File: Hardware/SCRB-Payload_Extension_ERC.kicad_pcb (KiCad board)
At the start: 4 copper layers, 83 parts, among them J1 Conn_01x03, J2 Conn_LoadCell, J3 ST_Link_Conn, J4 Conn_LoadCell, J5 Conn_LoadCell, J7 Conn_Therm, Q1 NMOS, SW1 SW_Tiny, U1 STM32F412RET6, U2 TPD4E05U06DQAR, U3 THVD1500DR, U4 ADS1220IPW, U5 ADS1220IPW, U6 ADS1220IPW, U7 INA241xxIDDFR, U8 TPD4E05U06DQAR, Y1 16M, 9p

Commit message: Updated ERC board schematic
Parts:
- added C1: 0.1uF, SCRB_STD_Passives:C0402, F.Cu at (227.9, 122.3)
- added C10: 510pF, SCRB_STD_Passives:C0402, F.Cu at (230.4, 123.9)
- added C11: 510nF, SCRB_STD_Passives:C0402, F.Cu at (230.4, 125.5)
- added C12: 0.1uF, SCRB_STD_Passives:C0402, F.Cu at (230.4, 127.1)
- added C13: 510pF, SCRB_STD_Passives:C0402, F.Cu at (230.4, 128.7)
- added C14: 0.1uF, SCRB_STD_Passives:C0402, F.Cu at (230.4, 130.4)
- added C15: 5.1nF, SCRB_STD_Passives:C0402, F.Cu at (230.4, 132.0)
- added C16: 12p, SCRB_STD_Passives:C0402, F.Cu at (232.9, 122.3)
- added C17: 510pF, SCRB_STD_Passives:C0402, F.Cu at (232.9, 123.9)
- added C19: 4.7uF, SCRB_STD_Passives:C0603, F.Cu at (212.4, 129.3)
- added C2: 0.1uF, SCRB_STD_Passives:C0402, F.Cu at (227.9, 123.9)
- added C20: 0.1u, SCRB_STD_Passives:C0402, F.Cu at (232.9, 125.5)
- added C21: 12p, SCRB_STD_Passives:C0402, F.Cu at (232.9, 127.1)
- added C24: 510pF, SCRB_STD_Passives:C0402, F.Cu at (232.9, 128.7)
- added C25: 5.1nF, SCRB_STD_Passives:C0402, F.Cu at (232.9, 130.4)
- added C26: 510pF, SCRB_STD_Passives:C0402, F.Cu at (232.9, 132.0)
- added C27: 0.1uF, SCRB_STD_Passives:C0402, F.Cu at (235.4, 122.3)
- added C28: 16nF, SCRB_STD_Passives:C0402, F.Cu at (235.4, 123.9)
- added C29: 0.1uF, SCRB_STD_Passives:C0402, F.Cu at (235.4, 125.5)
- added C3: 4.7uF, SCRB_STD_Passives:C0603, F.Cu at (212.4, 127.4)
- added C30: 0.1uF, SCRB_STD_Passives:C0402, F.Cu at (235.4, 127.1)
- added C31: 10nF, SCRB_STD_Passives:C0402, F.Cu at (235.4, 128.7)
- added C4: 0.1uF, SCRB_STD_Passives:C0402, F.Cu at (227.9, 125.5)
- added C5: 0.1uF, SCRB_STD_Passives:C0402, F.Cu at (227.9, 127.1)
- added C6: 0.1uF, SCRB_STD_Passives:C0402, F.Cu at (227.9, 128.7)
- added C7: 0.1uF, SCRB_STD_Passives:C0402, F.Cu at (227.9, 130.4)
- added C8: 6.8nF, SCRB_STD_Passives:C0402, F.Cu at (227.9, 132.0)
- added C9: 5.1nF, SCRB_STD_Passives:C0402, F.Cu at (230.4, 122.3)
- added H1: MountingHole, MountingHole:MountingHole_3.2mm_M3_DIN965_Pad, F.Cu at (196.3, 97.0)
- added H2: MountingHole, MountingHole:MountingHole_3.2mm_M3_DIN965_Pad, F.Cu at (196.3, 104.2)
- added H3: MountingHole, MountingHole:MountingHole_3.2mm_M3_DIN965_Pad, F.Cu at (196.3, 111.3)
- added H4: MountingHole, MountingHole:MountingHole_3.2mm_M3_DIN965_Pad, F.Cu at (196.3, 118.5)
- added IC1: STM32C542CCT6, SCRB_Misc_ICs:LQFP-48_7x7mm_P0.5mm, F.Cu at (205.3, 131.8)
- added J1: Conn_01x03, Connector_JST:JST_XH_B3B-XH-A_1x03_P2.50mm_Vertical, F.Cu at (217.8, 132.1)
- added J11: Conn_5V, SCRB_STD_Passives:R0402, F.Cu at (224.8, 108.7)
- added J2: Conn_LoadCell, Connector_JST:JST_XH_B4B-XH-A_1x04_P2.50mm_Vertical, F.Cu at (203.4, 96.8)
- added J4: Conn_LoadCell, Connector_JST:JST_XH_B4B-XH-A_1x04_P2.50mm_Vertical, F.Cu at (203.4, 104.6)
- added J5: Conn_LoadCell, Connector_JST:JST_XH_B4B-XH-A_1x04_P2.50mm_Vertical, F.Cu at (203.4, 112.4)
- added J7: Conn_Therm, Connector_JST:JST_GH_BM02B-GHS-TBT_1x02-1MP_P1.25mm_Vertical, F.Cu at (232.8, 97.3)
- added J8: ST-Link-Conn-SM, Connector_JST:JST_PH_B4B-PH-SM4-TB_1x04-1MP_P2.00mm_Vertical, F.Cu at (207.1, 122.1)
- added J9: Conn_20HIGH, Connector_AMASS:AMASS_XT30U-M_1x02_P5.0mm_Vertical, F.Cu at (218.0, 125.1)
- added LD1: LED0603, SCRB_STD_Actives:LED0603, F.Cu at (212.4, 131.3)
- added LD2: LED0603, SCRB_STD_Actives:LED0603, F.Cu at (212.4, 133.2)
- added Q1: NMOS, SCRB_STD_Actives:SOT-23, F.Cu at (228.8, 134.7)
- added R1: 10k, SCRB_STD_Passives:R0402, F.Cu at (224.8, 110.4)
- added R10: 470, SCRB_STD_Passives:R0402, F.Cu at (227.3, 113.7)
- added R11: 10k, SCRB_STD_Passives:R0402, F.Cu at (227.3, 115.3)
- added R12: 47, SCRB_STD_Passives:R0402, F.Cu at (227.3, 116.9)
- added R13: 47, SCRB_STD_Passives:R0402, F.Cu at (229.9, 108.7)
- added R14: 47, SCRB_STD_Passives:R0402, F.Cu at (229.9, 110.4)
- added R15: 47, SCRB_STD_Passives:R0402, F.Cu at (229.9, 112.0)
- added R16: 47, SCRB_STD_Passives:R0402, F.Cu at (229.9, 113.7)
- added R17: 47, SCRB_STD_Passives:R0402, F.Cu at (229.9, 115.3)
- added R18: 47, SCRB_STD_Passives:R0402, F.Cu at (229.9, 116.9)
- added R19: 47, SCRB_STD_Passives:R0402, F.Cu at (232.4, 108.7)
- added R2: 120, SCRB_STD_Passives:R0805, F.Cu at (225.4, 119.0)
- added R20: 47, SCRB_STD_Passives:R0402, F.Cu at (232.4, 110.4)
- added R21: 47, SCRB_STD_Passives:R0402, F.Cu at (232.4, 112.0)
- added R22: 47, SCRB_STD_Passives:R0402, F.Cu at (232.4, 113.7)
- added R23: 47, SCRB_STD_Passives:R0402, F.Cu at (232.4, 115.3)
- added R24: 4.7k, SCRB_STD_Passives:R0402, F.Cu at (232.4, 116.9)
- added R25: 4.7k, SCRB_STD_Passives:R0402, F.Cu at (235.0, 108.7)
- added R26: 470, SCRB_STD_Passives:R0402, F.Cu at (235.0, 110.4)
- added R27: 10k, SCRB_STD_Passives:R0402, F.Cu at (235.0, 112.0)
- added R28: 100, SCRB_STD_Passives:R0402, F.Cu at (235.0, 113.7)
- added R29: 270, SCRB_STD_Passives:R0402, F.Cu at (235.0, 115.3)
- added R3: 470, SCRB_STD_Passives:R0402, F.Cu at (224.8, 112.0)
- added R30: 10m, SCRB_STD_Passives:R0603, F.Cu at (212.4, 135.2)
- added R31: 470, SCRB_STD_Passives:R0402, F.Cu at (235.0, 116.9)
- added R4: 470, SCRB_STD_Passives:R0402, F.Cu at (224.8, 113.7)
- added R5: 100, SCRB_STD_Passives:R0402, F.Cu at (224.8, 115.3)
- added R6: 100, SCRB_STD_Passives:R0402, F.Cu at (224.8, 116.9)
- added R7: 10k, SCRB_STD_Passives:R0402, F.Cu at (227.3, 108.7)
- added R8: 4.7k, SCRB_STD_Passives:R0402, F.Cu at (227.3, 110.4)
- added R9: 470, SCRB_STD_Passives:R0402, F.Cu at (227.3, 112.0)
- added SW1: SW_Tiny, SCRB_Electromechanical:SW_C913791, F.Cu at (194.8, 135.6)
- added TP1: Testpoint, TestPoint:TestPoint_Loop_D2.60mm_Drill1.6mm_Beaded, F.Cu at (195.3, 124.6)
- added U1: STM32F412RET6, Package_QFP:LQFP-64_10x10mm_P0.5mm, F.Cu at (221.6, 100.7)
- added U2: TPD4E05U06DQAR, SCRB_TexasInstruments:DQA0010A, F.Cu at (193.9, 128.9)
- added U3: THVD1500DR, SCRB_TexasInstruments:D0008A, F.Cu at (232.8, 104.1)
- added U4: ADS1220IPW, ADS1220:PW16, F.Cu at (218.8, 111.3)
- added U5: ADS1220IPW, ADS1220:PW16, F.Cu at (218.8, 118.1)
- added U7: INA241A4IDDFR, SCRB_TexasInstruments:DDF0008A, F.Cu at (233.1, 134.7)
- added U8: TPD4E05U06DQAR, SCRB_TexasInstruments:DQA0010A, F.Cu at (196.3, 128.9)
- added Y1: 16M, 9p, SCRB_STD_Passives:SMD3225, F.Cu at (195.1, 132.5)

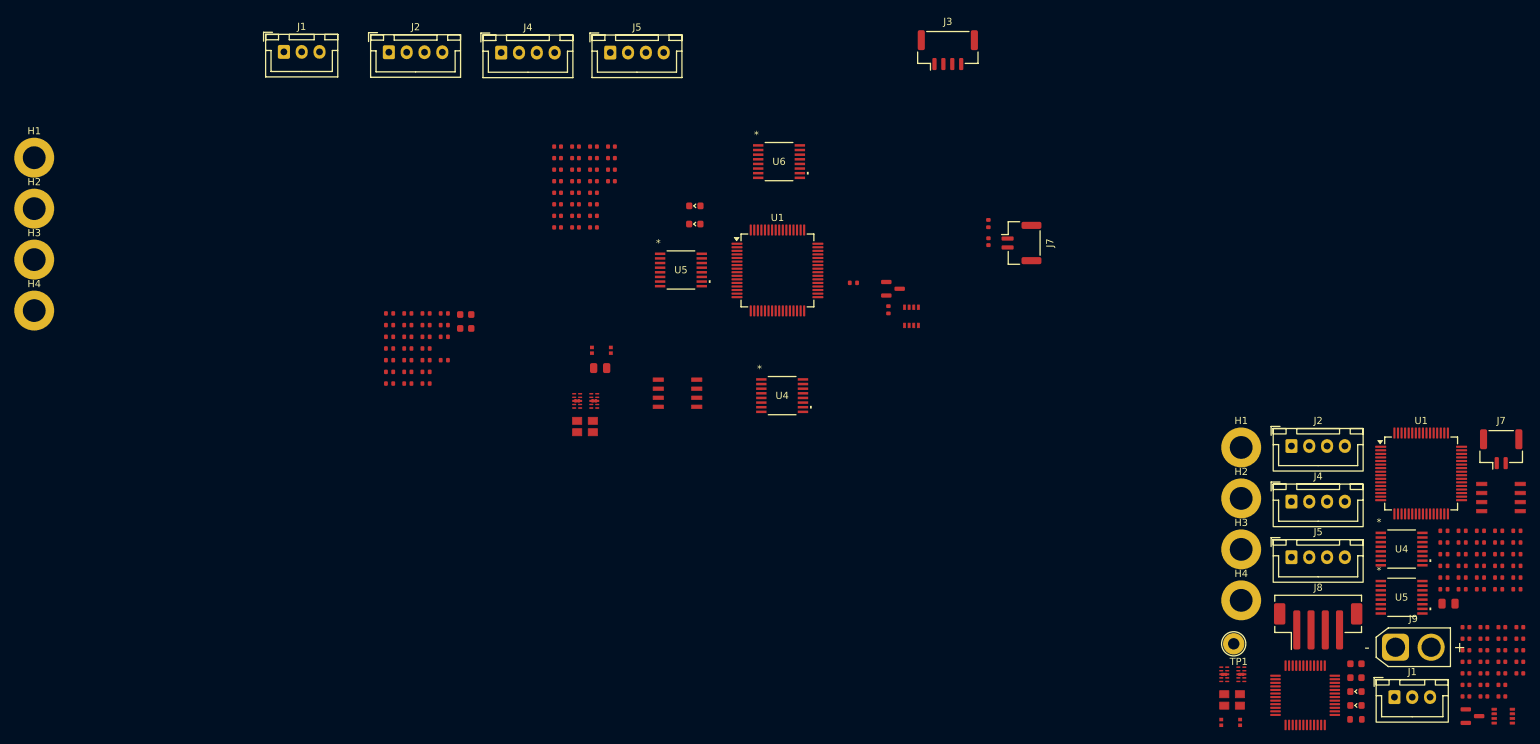
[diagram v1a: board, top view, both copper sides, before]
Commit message: added extra load cell on schematic
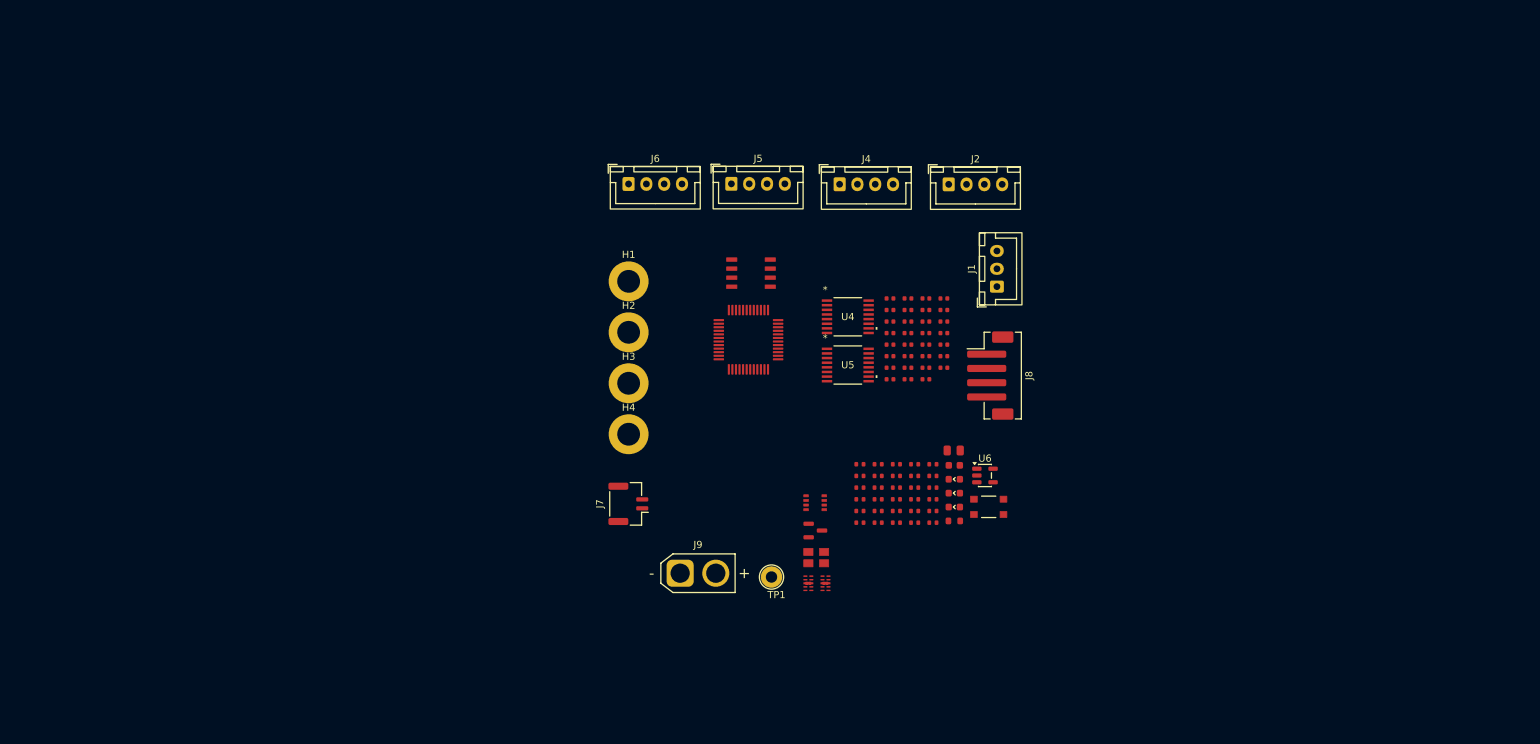
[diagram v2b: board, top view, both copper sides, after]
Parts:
- removed the C1 at (227.9, 122.3)
- removed the C1 at (100.4, 54.8)
- removed the C10 at (230.4, 123.9)
- removed the C10 at (102.9, 54.8)
- removed the C11 at (102.9, 56.5)
- removed the C11 at (230.4, 125.5)
- removed the C12 at (230.4, 127.1)
- removed the C12 at (102.9, 58.1)
- removed the C13 at (230.4, 128.7)
- removed the C13 at (102.9, 59.7)
- removed C14 (x2), C4 (x2), C5 (x2), C6 (x2): 0.1uF, SCRB_STD_Passives:C0402
- removed the C15 at (230.4, 132.0)
- removed the C15 at (102.9, 62.9)
- removed the C16 at (232.9, 122.3)
- removed the C16 at (102.9, 64.5)
- removed the C17 at (232.9, 123.9)
- removed the C17 at (102.9, 66.2)
- removed C19 (x2), C3 (x2): 4.7uF, SCRB_STD_Passives:C0603
- removed the C2 at (227.9, 123.9)
- removed the C2 at (100.4, 56.5)
- removed the C20 at (232.9, 125.5)
- removed the C20 at (105.5, 56.5)
- removed the C21 at (232.9, 127.1)
- removed the C21 at (105.5, 58.1)
- removed the C24 at (105.5, 62.9)
- removed the C24 at (232.9, 128.7)
- removed the C25 at (232.9, 130.4)
- removed the C25 at (105.5, 64.5)
- removed the C26 at (232.9, 132.0)
- removed the C26 at (105.5, 66.2)
- removed the C27 at (108.0, 54.8)
- removed the C27 at (235.4, 122.3)
- removed C28: 16nF, SCRB_STD_Passives:C0402
- removed C28: 5.1nF, SCRB_STD_Passives:C0402
- removed the C29 at (108.0, 58.1)
- removed the C29 at (235.4, 125.5)
- removed the C30 at (108.0, 59.7)
- removed the C30 at (235.4, 127.1)
- removed the C31 at (160.9, 68.2)
- removed the C31 at (235.4, 128.7)
- removed the C7 at (227.9, 130.4)
- removed the C7 at (100.4, 62.9)
- removed the C8 at (100.4, 64.5)
- removed the C8 at (227.9, 132.0)
- removed the C9 at (230.4, 122.3)
- removed the C9 at (100.4, 66.2)
- removed the H1 at (27.0, 56.4)
- removed the H1 at (196.3, 97.0)
- removed the H2 at (27.0, 63.5)
- removed the H2 at (196.3, 104.2)
- removed the H3 at (27.0, 70.7)
- removed the H3 at (196.3, 111.3)
- removed the H4 at (196.3, 118.5)
- removed the H4 at (27.0, 77.8)
- removed the J1 at (217.8, 132.1)
- removed the J1 at (62.0, 41.5)
- removed the J2 at (203.4, 96.8)
- removed the J2 at (76.7, 41.6)
- removed J3: ST_Link_Conn, Connector_JST:JST_GH_BM04B-GHS-TBT_1x04-1MP_P1.25mm_Vertical
- removed the J4 at (203.4, 104.6)
- removed the J4 at (92.5, 41.6)
- removed the J5 at (107.8, 41.6)
- removed the J5 at (203.4, 112.4)
- removed the J7 at (232.8, 97.3)
- removed the J7 at (165.5, 68.4)
- removed the LD1 at (119.7, 63.1)
- removed the LD1 at (212.4, 131.3)
- removed the LD2 at (212.4, 133.2)
- removed the LD2 at (119.7, 65.7)
- removed the Q1 at (228.8, 134.7)
- removed the Q1 at (147.5, 74.8)
- removed the R1 at (76.8, 78.2)
- removed the R1 at (224.8, 110.4)
- removed the R10 at (79.4, 79.9)
- removed the R10 at (227.3, 113.7)
- removed the R11 at (227.3, 115.3)
- removed the R11 at (79.4, 81.5)
- removed the R12 at (79.4, 83.2)
- removed the R12 at (227.3, 116.9)
- removed R13 (x2), R14 (x2), R15 (x2), R16 (x2), R17 (x2), R18 (x2), R19 (x2), R20 (x2), R21 (x2), R22 (x2), R23 (x2): 47, SCRB_STD_Passives:R0402
- removed the R2 at (225.4, 119.0)
- removed the R2 at (106.4, 85.9)
- removed R24 (x2), R25 (x2): 4.7k, SCRB_STD_Passives:R0402
- removed the R26 at (146.8, 77.7)
- removed the R26 at (235.0, 110.4)
- removed the R27 at (235.0, 112.0)
- removed the R27 at (84.5, 84.8)
- removed the R28 at (141.9, 74.0)
- removed the R28 at (235.0, 113.7)
- removed the R29 at (235.0, 115.3)
- removed the R29 at (160.9, 65.6)
- removed the R3 at (224.8, 112.0)
- removed the R3 at (76.8, 79.9)
- removed the R4 at (224.8, 113.7)
- removed the R4 at (76.8, 81.5)
- removed the R5 at (224.8, 115.3)
- removed the R5 at (76.8, 83.2)
- removed the R6 at (224.8, 116.9)
- removed the R6 at (76.8, 84.8)
- removed the R7 at (76.8, 86.4)
- removed the R7 at (227.3, 108.7)
- removed the R8 at (76.8, 88.1)
- removed the R8 at (227.3, 110.4)
- removed the R9 at (227.3, 112.0)
- removed the R9 at (79.4, 78.2)
- removed the SW1 at (106.6, 83.4)
- removed the SW1 at (194.8, 135.6)
- removed U1 (x2): STM32F412RET6, Package_QFP:LQFP-64_10x10mm_P0.5mm
- removed the U2 at (193.9, 128.9)
- removed the U2 at (103.2, 90.5)
- removed the U3 at (117.2, 89.4)
- removed the U3 at (232.8, 104.1)
- removed the U4 at (218.8, 111.3)
- removed the U4 at (131.9, 89.8)
- removed the U5 at (218.8, 118.1)
- removed the U5 at (117.7, 72.1)
- removed the U7 at (150.1, 78.7)
- removed the U7 at (233.1, 134.7)
- removed the U8 at (105.6, 90.5)
- removed the U8 at (196.3, 128.9)
- removed the Y1 at (195.1, 132.5)
- removed the Y1 at (104.3, 94.1)
- added C1: 0.1uF, SCRB_STD_Passives:C0402, F.Cu at (147.1, 76.1)
- added C10: 510pF, SCRB_STD_Passives:C0402, F.Cu at (147.1, 84.2)
- added C11: 510nF, SCRB_STD_Passives:C0402, F.Cu at (147.1, 85.9)
- added C12: 6.8nF, SCRB_STD_Passives:C0402, F.Cu at (147.1, 87.5)
- added C13: 510pF, SCRB_STD_Passives:C0402, F.Cu at (149.6, 76.1)
- added C15: 5.1nF, SCRB_STD_Passives:C0402, F.Cu at (149.6, 77.8)
- added C16: 12p, SCRB_STD_Passives:C0402, F.Cu at (149.6, 79.4)
- added C17: 510pF, SCRB_STD_Passives:C0402, F.Cu at (149.6, 81.0)
- added C2: 0.1uF, SCRB_STD_Passives:C0402, F.Cu at (147.1, 77.8)
- added C20: 0.1u, SCRB_STD_Passives:C0402, F.Cu at (149.6, 84.2)
- added C21: 12p, SCRB_STD_Passives:C0402, F.Cu at (149.6, 85.9)
- added C24: 510pF, SCRB_STD_Passives:C0402, F.Cu at (152.1, 77.8)
- added C25: 5.1nF, SCRB_STD_Passives:C0402, F.Cu at (152.1, 79.4)
- added C26: 510pF, SCRB_STD_Passives:C0402, F.Cu at (152.1, 81.0)
- added C27: 0.1uF, SCRB_STD_Passives:C0402, F.Cu at (152.1, 82.6)
- added C29: 0.1uF, SCRB_STD_Passives:C0402, F.Cu at (152.1, 84.2)
- added C30: 0.1uF, SCRB_STD_Passives:C0402, F.Cu at (152.1, 85.9)
- added C31: 510pF, SCRB_STD_Passives:C0402, F.Cu at (152.1, 87.5)
- added C32: 0.1uF, SCRB_STD_Passives:C0402, F.Cu at (154.6, 76.1)
- added C33: 0.1unF, SCRB_STD_Passives:C0402, F.Cu at (154.6, 77.8)
- added C34: 4.7uF, SCRB_STD_Passives:C0402, F.Cu at (154.6, 79.4)
- added C35: 2.2uF, SCRB_STD_Passives:C0603, F.Cu at (156.1, 99.6)
- added C36: 0.1uF, SCRB_STD_Passives:C0402, F.Cu at (154.6, 81.0)
- added C37: 10nF, SCRB_STD_Passives:C0402, F.Cu at (154.6, 82.6)
- added C38: 5.1nF, SCRB_STD_Passives:C0402, F.Cu at (154.6, 84.2)
- added C39: 510pF, SCRB_STD_Passives:C0402, F.Cu at (154.6, 85.9)
- added C7: 0.1uF, SCRB_STD_Passives:C0402, F.Cu at (147.1, 79.4)
- added C8: 6.8nF, SCRB_STD_Passives:C0402, F.Cu at (147.1, 81.0)
- added C9: 5.1nF, SCRB_STD_Passives:C0402, F.Cu at (147.1, 82.6)
- added H1: MountingHole, MountingHole:MountingHole_3.2mm_M3_DIN965_Pad, F.Cu at (110.4, 73.7)
- added H2: MountingHole, MountingHole:MountingHole_3.2mm_M3_DIN965_Pad, F.Cu at (110.4, 80.9)
- added H3: MountingHole, MountingHole:MountingHole_3.2mm_M3_DIN965_Pad, F.Cu at (110.4, 88.0)
- added H4: MountingHole, MountingHole:MountingHole_3.2mm_M3_DIN965_Pad, F.Cu at (110.4, 95.2)
- added J1: Conn_01x03, Connector_JST:JST_XH_B3B-XH-A_1x03_P2.50mm_Vertical, F.Cu at (162.1, 74.5)
- added J2: Conn_LoadCell, Connector_JST:JST_XH_B4B-XH-A_1x04_P2.50mm_Vertical, F.Cu at (155.3, 60.1)
- added J4: Conn_LoadCell, Connector_JST:JST_XH_B4B-XH-A_1x04_P2.50mm_Vertical, F.Cu at (140.0, 60.1)
- added J5: Conn_LoadCell, Connector_JST:JST_XH_B4B-XH-A_1x04_P2.50mm_Vertical, F.Cu at (124.8, 60.1)
- added J6: Conn_LoadCell, Connector_JST:JST_XH_B4B-XH-A_1x04_P2.50mm_Vertical, F.Cu at (110.4, 60.1)
- added J7: Conn_Therm, Connector_JST:JST_GH_BM02B-GHS-TBT_1x02-1MP_P1.25mm_Vertical, F.Cu at (110.3, 105.0)
- added LD1: LED0603, SCRB_STD_Actives:LED0603, F.Cu at (156.1, 101.5)
- added LD2: LED0603, SCRB_STD_Actives:LED0603, F.Cu at (156.1, 103.5)
- added LD3: LED0603, SCRB_STD_Actives:LED0603, F.Cu at (156.1, 105.4)
- added Q1: NMOS, SCRB_STD_Actives:SOT-23, F.Cu at (136.6, 108.7)
- added R1: 10k, SCRB_STD_Passives:R0402, F.Cu at (142.8, 101.0)
- added R10: 470, SCRB_STD_Passives:R0402, F.Cu at (145.4, 104.3)
- added R11: 470, SCRB_STD_Passives:R0402, F.Cu at (145.4, 106.0)
- added R12: 470, SCRB_STD_Passives:R0402, F.Cu at (145.4, 107.6)
- added R2: 120, SCRB_STD_Passives:R0805, F.Cu at (156.0, 97.5)
- added R26: 470, SCRB_STD_Passives:R0402, F.Cu at (147.9, 99.4)
- added R27: 10k, SCRB_STD_Passives:R0402, F.Cu at (147.9, 101.0)
- added R28: 100, SCRB_STD_Passives:R0402, F.Cu at (147.9, 102.7)
- added R29: 270, SCRB_STD_Passives:R0402, F.Cu at (147.9, 104.3)
- added R3: 470, SCRB_STD_Passives:R0402, F.Cu at (142.8, 102.7)
- added R32: 10k, SCRB_STD_Passives:R0402, F.Cu at (147.9, 107.6)
- added R33: 47, SCRB_STD_Passives:R0402, F.Cu at (150.5, 99.4)
- added R34: 47, SCRB_STD_Passives:R0402, F.Cu at (150.5, 101.0)
- added R35: 47, SCRB_STD_Passives:R0402, F.Cu at (150.5, 102.7)
- added R36: 47, SCRB_STD_Passives:R0402, F.Cu at (150.5, 104.3)
- added R37: 47, SCRB_STD_Passives:R0402, F.Cu at (150.5, 106.0)
- added R38: 47, SCRB_STD_Passives:R0402, F.Cu at (150.5, 107.6)
- added R39: 47, SCRB_STD_Passives:R0402, F.Cu at (153.1, 99.4)
- added R4: 470, SCRB_STD_Passives:R0402, F.Cu at (142.8, 104.3)
- added R40: 47, SCRB_STD_Passives:R0402, F.Cu at (153.1, 101.0)
- added R41: 4.7K, SCRB_STD_Passives:R0402, F.Cu at (153.1, 102.7)
- added R42: 4.7K, SCRB_STD_Passives:R0402, F.Cu at (153.1, 104.3)
- added R43: 470, SCRB_STD_Passives:R0402, F.Cu at (153.1, 106.0)
- added R44: 470, SCRB_STD_Passives:R0402, F.Cu at (153.1, 107.6)
- added R5: 100, SCRB_STD_Passives:R0402, F.Cu at (142.8, 106.0)
- added R6: 100, SCRB_STD_Passives:R0402, F.Cu at (142.8, 107.6)
- added R7: 10k, SCRB_STD_Passives:R0402, F.Cu at (145.4, 99.4)
- added R8: 4.7k, SCRB_STD_Passives:R0402, F.Cu at (145.4, 101.0)
- added R9: 470, SCRB_STD_Passives:R0402, F.Cu at (145.4, 102.7)
- added SW1: SW_Oval, SCRB_Electromechanical:SW_C2888430, F.Cu at (160.9, 105.4)
- added U2: TPD4E05U06DQAR, SCRB_TexasInstruments:DQA0010A, F.Cu at (135.6, 116.1)
- added U3: THVD1500DR, SCRB_TexasInstruments:D0008A, F.Cu at (127.5, 72.6)
- added U4: ADS1220IPW, ADS1220:PW16, F.Cu at (141.1, 78.7)
- added U5: ADS1220IPW, ADS1220:PW16, F.Cu at (141.1, 85.5)
- added U7: INA241A4IDDFR, SCRB_TexasInstruments:DDF0008A, F.Cu at (136.6, 104.8)
- added U8: TPD4E05U06DQAR, SCRB_TexasInstruments:DQA0010A, F.Cu at (138.0, 116.1)
- added Y1: 16M, 9p, SCRB_STD_Passives:SMD3225, F.Cu at (136.7, 112.5)
- C18: value 0.1uF -> 1uF
- C22: value 5.1nF -> 0.1uF
- U6: value ADS1220IPW -> TLV75533PDBV; footprint ADS1220:PW16 -> Package_TO_SOT_SMD:SOT-23-5
- moved J9 100.9 mm to (117.6, 114.7)
- moved IC1 92.7 mm to (127.2, 81.9)
- moved R31 87.7 mm to (147.9, 106.0)
- moved J11 82.5 mm to (142.8, 99.4)
- moved TP1 65.5 mm to (130.4, 115.2)
- moved R30 62.9 mm to (156.1, 107.4)
- moved J8 57.9 mm to (161.1, 87.0), turned to -90 degrees
- moved U6 52.7 mm to (160.4, 101.0)
- moved C18 52.1 mm to (149.6, 82.6)
- moved C22 52.1 mm to (149.6, 87.5)
- moved C23 48.9 mm to (152.1, 76.1)
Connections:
- C22 pad 1: /5V -> /3V3
- C22 pad 2: /E2- -> GND
- C23 pad 1: /3V3 -> GND
- C23 pad 2: GND -> /3V3
- IC1 pad 1: unconnected-(IC1-PE2-Pad1) -> /LED_RUN
- IC1 pad 11: unconnected-(IC1-PA1-Pad11) -> /ADC_Therm
- IC1 pad 12: unconnected-(IC1-PA2-Pad12) -> /CURR_VOUT
- IC1 pad 13: unconnected-(IC1-PA3-Pad13) -> Net-(IC1-PA3)
- IC1 pad 14: unconnected-(IC1-PA4-Pad14) -> Net-(IC1-PA4)
- IC1 pad 15: unconnected-(IC1-PA5-Pad15) -> Net-(IC1-PA5)
- IC1 pad 16: unconnected-(IC1-PA6-Pad16) -> Net-(IC1-PA6)
- IC1 pad 17: unconnected-(IC1-PA7-Pad17) -> Net-(IC1-PA7)
- IC1 pad 19: unconnected-(IC1-PB1-Pad19) -> Net-(IC1-PB1)
- IC1 pad 2: unconnected-(IC1-PC13-Pad2) -> /LED_PANIK
- IC1 pad 20: unconnected-(IC1-PB2-Pad20) -> Net-(IC1-PB2)
- IC1 pad 21: unconnected-(IC1-PB10-Pad21) -> Net-(IC1-PB10)
- IC1 pad 22: unconnected-(IC1-VCAP-Pad22) -> Net-(IC1-VCAP)
- IC1 pad 23: unconnected-(IC1-VSS_1-Pad23) -> GND
- IC1 pad 24: unconnected-(IC1-VDD_1-Pad24) -> /3V3
- IC1 pad 25: unconnected-(IC1-PB12-Pad25) -> /UART_RX
- IC1 pad 26: unconnected-(IC1-PB13-Pad26) -> /UART_TX
- IC1 pad 29: unconnected-(IC1-PA8-Pad29) -> /GATE_SW
- IC1 pad 34: unconnected-(IC1-PA13-Pad34) -> /SYS_SWDIO
- IC1 pad 35: unconnected-(IC1-VSS_2-Pad35) -> GND
- IC1 pad 36: unconnected-(IC1-VDD_2-Pad36) -> /3V3
- IC1 pad 37: unconnected-(IC1-PA14-Pad37) -> /SYS_SWDCLK
- IC1 pad 47: unconnected-(IC1-VSS_3-Pad47) -> GND
- IC1 pad 48: unconnected-(IC1-VDD_3-Pad48) -> /3V3
- IC1 pad 5: unconnected-(IC1-PH0-OSC_IN-Pad5) -> /RCC_OSC_IN
- IC1 pad 6: unconnected-(IC1-PH1-OSC_OUT-Pad6) -> /RCC_OSC_OUT
- IC1 pad 7: unconnected-(IC1-NRST-Pad7) -> /NRST
- IC1 pad 8: unconnected-(IC1-VREF--Pad8) -> GND
- IC1 pad 9: unconnected-(IC1-VREF+-Pad9) -> Net-(IC1-VREF+)
- U6 pad 1: /SPI3_SCK -> /5V
- U6 pad 2: /SPI3_~{CS} -> GND
- U6 pad 3: GND -> /5V
- U6 pad 4: GND -> unconnected-(U6-NC-Pad4)
- U6 pad 5: GND -> /3V3

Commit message: working on buck converter wiring
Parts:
- added IC2: AOZ2260AQI-15, AOZ2260AQI-15:AOZ2260AQI15, F.Cu at (155.2, 70.1)
- R29: value 270 -> 680
- moved J2 37.5 mm to (119.0, 69.7)
- moved U3 36.1 mm to (119.5, 107.8)
- moved SW1 34.3 mm to (126.6, 107.0)
- moved J6 34.2 mm to (119.0, 93.1)
- moved J1 31.1 mm to (149.8, 103.1), turned to 0 degrees
- moved J7 30.8 mm to (141.1, 106.2), turned to 0 degrees
- moved U6 27.8 mm to (132.6, 102.4)
- moved IC1 27.4 mm to (151.7, 94.3)
- moved J4 27.3 mm to (119.0, 77.5)
- moved R2 26.9 mm to (131.9, 109.5)
- moved J5 25.9 mm to (119.0, 85.3)
- moved H1 23.5 mm to (133.6, 69.9)
- moved H2 23.5 mm to (133.6, 77.1)
- moved H3 23.5 mm to (133.6, 84.2)
- moved H4 23.5 mm to (133.6, 91.4)
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
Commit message: PCB layout in progress
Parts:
- removed C34: 4.7uF, SCRB_STD_Passives:C0402
- removed IC2: AOZ2260AQI-15, AOZ2260AQI-15:AOZ2260AQI15
- added C14: 0.1u, SCRB_STD_Passives:C0402, F.Cu at (205.5, 82.8)
- added C3: 10u, SCRB_STD_Passives:C0402, F.Cu at (192.1, 78.4)
- added C4: 68u, SCRB_STD_Passives:C0603, F.Cu at (189.2, 78.5)
- added C5: 20p, SCRB_STD_Passives:C0402, F.Cu at (192.1, 80.0)
- added C6: 4.7u, SCRB_STD_Passives:C0603, F.Cu at (125.0, 80.3)
- added D1: D_Zener, Diode_THT:D_DO-41_SOD81_P10.16mm_Horizontal, F.Cu at (186.7, 75.4)
- added D2: SMBJ6.0CA, SCRB_STD_Actives:SMB, F.Cu at (144.9, 104.9)
- added L1: 3.7u, SCRB_STD_Passives:L0805, F.Cu at (195.4, 78.7)
- added R13: 121k, SCRB_STD_Passives:R0402, F.Cu at (186.1, 78.4)
- added R14: 54.9k, SCRB_STD_Passives:R0402, F.Cu at (186.1, 80.0)
- added R15: 18k, SCRB_STD_Passives:R0402, F.Cu at (201.4, 79.9)
- added R16: 30k, SCRB_STD_Passives:R0603, F.Cu at (189.2, 80.5)
- added R17: 45k, SCRB_STD_Passives:R0603, F.Cu at (204.4, 80.7)
- added R18: 100k, SCRB_STD_Passives:R0402, F.Cu at (201.4, 81.6)
- added R19: R0402, SCRB_STD_Passives:R0402, F.Cu at (201.4, 83.2)
- added SB1: SB0402, SCRB_STD_Passives:JP0402_NO, F.Cu at (147.8, 98.7)
- added U1: TPS543x21, TPS54x38:VQFN-HR9_RQF_TEX, F.Cu at (204.0, 75.7)
- C33: value 0.1unF -> 0.1uF
- H1, H2, H3, H4: footprint MountingHole:MountingHole_3.2mm_M3_DIN965_Pad -> MountingHole:MountingHole_3.2mm_M3
- J1: value Conn_01x03 -> Conn_UART
- J11: footprint SCRB_STD_Passives:R0402 -> Connector_JST:JST_XH_B2B-XH-AM_1x02_P2.50mm_Vertical
- J2, J4, J5, J6: footprint Connector_JST:JST_XH_B4B-XH-A_1x04_P2.50mm_Vertical -> Connector_JST:JST_PH_B4B-PH-SM4-TB_1x04-1MP_P2.00mm_Vertical
- J9: value Conn_20HIGH -> Conn_6HIGH
- LD3: value LED0603 -> 3V3_LED
- moved J6 54.8 mm to (172.5, 104.8), turned to -90 degrees
- moved J5 53.8 mm to (172.5, 91.0), turned to -90 degrees
- moved J4 53.5 mm to (172.5, 77.2), turned to -90 degrees
- moved R41 53.4 mm to (117.5, 114.0), turned to 180 degrees
- moved H3 51.3 mm to (174.5, 115.2)
- moved R1 47.5 mm to (114.1, 111.1), turned to 180 degrees
- moved U8 45.0 mm to (125.5, 74.7), turned to -90 degrees
- moved LD2 42.3 mm to (118.0, 82.7), turned to 180 degrees
- moved LD1 42.2 mm to (118.0, 81.1), turned to 180 degrees
- moved H2 42.2 mm to (174.5, 66.9)
- moved J9 39.1 mm to (156.3, 113.4)
- moved J7 38.4 mm to (140.5, 67.8)
- moved Q1 38.1 mm to (158.7, 72.8)
- moved H4 37.9 mm to (104.1, 115.2)
- moved R8 36.5 mm to (114.8, 82.7)
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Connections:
- net /20_Hi renamed /6_Hi
- C22 pad 1: /3V3 -> /ldo_3V3
- J11 pad 1: /5V -> /tvs_5V
- J9 pad 2: 20_Lo -> GND
- R11 pad 1: unconnected-(R11-Pad1) -> /Sig4+
- R12 pad 1: unconnected-(R12-Pad1) -> /Sig4-
- R30 pad 2: 20_Lo -> 6_Lo
- R32 pad 1: /3V3 -> /ldo_3V3
- U6 pad 5: /3V3 -> /ldo_3V3
- U7 pad 1: 20_Lo -> 6_Lo
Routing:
- net /5V: track 0.00 -> 49.0 mm, vias 0 -> 7
- net GND: track 0.00 -> 40.3 mm, vias 0 -> 34
- net /3V3: track 0.00 -> 32.3 mm, vias 0 -> 7
- net /ADC_Therm: track 0.00 -> 29.0 mm, vias 0 -> 2
- net /NRST: track 0.00 -> 24.3 mm, vias 0 -> 2
- net /RCC_OSC_IN: track 0.00 -> 10.1 mm
- net /RCC_OSC_OUT: track 0.00 -> 10.1 mm
- net /RS485A: track 0.00 -> 8.94 mm
- net /RS485B: track 0.00 -> 8.88 mm
- net /LED_RUN: track 0.00 -> 7.15 mm
- net /LED_PANIK: track 0.00 -> 6.73 mm
- net /tvs_5V: track 0.00 -> 6.53 mm
- net /SYS_SWDCLK: track 0.00 -> 5.84 mm
- net /SYS_SWDIO: track 0.00 -> 5.78 mm
- net /AIN0_1: track 0.00 -> 5.19 mm
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- added copper zone on In2.Cu, net /3V3
- added copper zone on In2.Cu, net /5V
- added copper zone on F.Cu, net /6_Hi
- added copper zone on In1.Cu, net /6_Hi
- added copper zone on In1.Cu, net GND
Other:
- board outline added: 79.3 x 57.3 mm
- board text added: "PANIK"
- board text added: "RUN"
- board text added: "SCRB-SP-27-00-02-ERC-Board"
- board text added: "⠀⠀⠀⠀⠀⠀⠀⢀⣀⡤⠴⠶⠶⠒⠲⠦⢤⣀⠀⠀⠀⠀⠀⠀⠀⠀⠀⠀ ⠀⠀⠀⠀⢀⡠⠞⠋⠀⠀⠀⠀⠀⠀⠀⠀⠀⠈⠉⠲⠤⣄⡀⠀⠀⠀⠀⠀ ⠀⠀⣀⡴⠋⠀⠀⠀⠀⠀⠀⠀⠀⠀⠀⠀⠀⠀⠀⠀⠀⣤⡿⠀⠀⠀⠀⠀ ⠀⢾⣅⡀⠀⠀⠀⠀⣀⠀⠀⠀⠀⠀⠀⢀⡦⠤⠄⠀⠀⢻⡀⠀⠀⠀⠀⠀ ⠀⠈⢹⡏⠀⠀⠐⠋⠉⠁⠀⠻⢿⠟⠁⠀⠀⢤⠀⠀⠠⠤⢷⣤⣤⢤⡄⠀ ⠀⠀⣼⡤⠤⠀⠀⠘⣆⡀⠀⣀⡼⠦⣄⣀⡤⠊⠀⠀⠀⠤⣼⠟⠀⠀⢹⡂ ⠀⠊⣿⡠⠆⠀⠀⠀⠈⠉⠉⠙⠤⠤⠋⠀⠀⠀⠀⠀⠀⡰⠋⠀⠀⠀⡼⠁ ⠀⢀⡾⣧⡀⠀⠀⠀⠀⠀⠀⠀⠀⠀⠀⠀⠀⠀⠀⠀⠜⠁⠀⠀⠀⣸⠁⠀ ⠀⠀⠀⡼⠙⠢⠀⠀⠀⠀⠀⠀⠀⠀⠀⠀⠀⠀⠀⠀⠀⠀⠀⠀⣰⠃⠀⠀ ⠀⢀⡞⠁⠀⠀⠀⠀⠀⠀⠀⠀⠀⠀⠀⠀⠀⠀⠀⠀⠀⠀⠀⣰⠃⠀⠀⠀ ⠀⡼⠀⠀⠀⠀⠀⠀⠀⠀⠀⠀⠀⠀⠀⠀⠀⠀⠀⠀⠀⠀⠀⡇⠀⠀⠀⠀ ⣾⠁⠀⢀⣠⡴⠆⠀⠀⠀⠀⠀⠀⠀⠀⠀⠀⠀⠀⠀⠀⠀⠀⡇⠀⠀⠀⠀ ⠈⠛⠻⠉⠀⠀⠀⠀⠀⠀⠀⠀⠀⠀⠀⠀⠀⠀⠀⠀⠀⠀⠀⡇⠀⠀⠀⠀"
